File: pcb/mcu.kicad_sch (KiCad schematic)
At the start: 24 parts, among them J1 Conn_01x02_Pin, SW1 SW_Push, U1 STM32H750VBTx, U2 W25Q64JVSSIQ_C179171, U3 TLV1117LV33DCYR

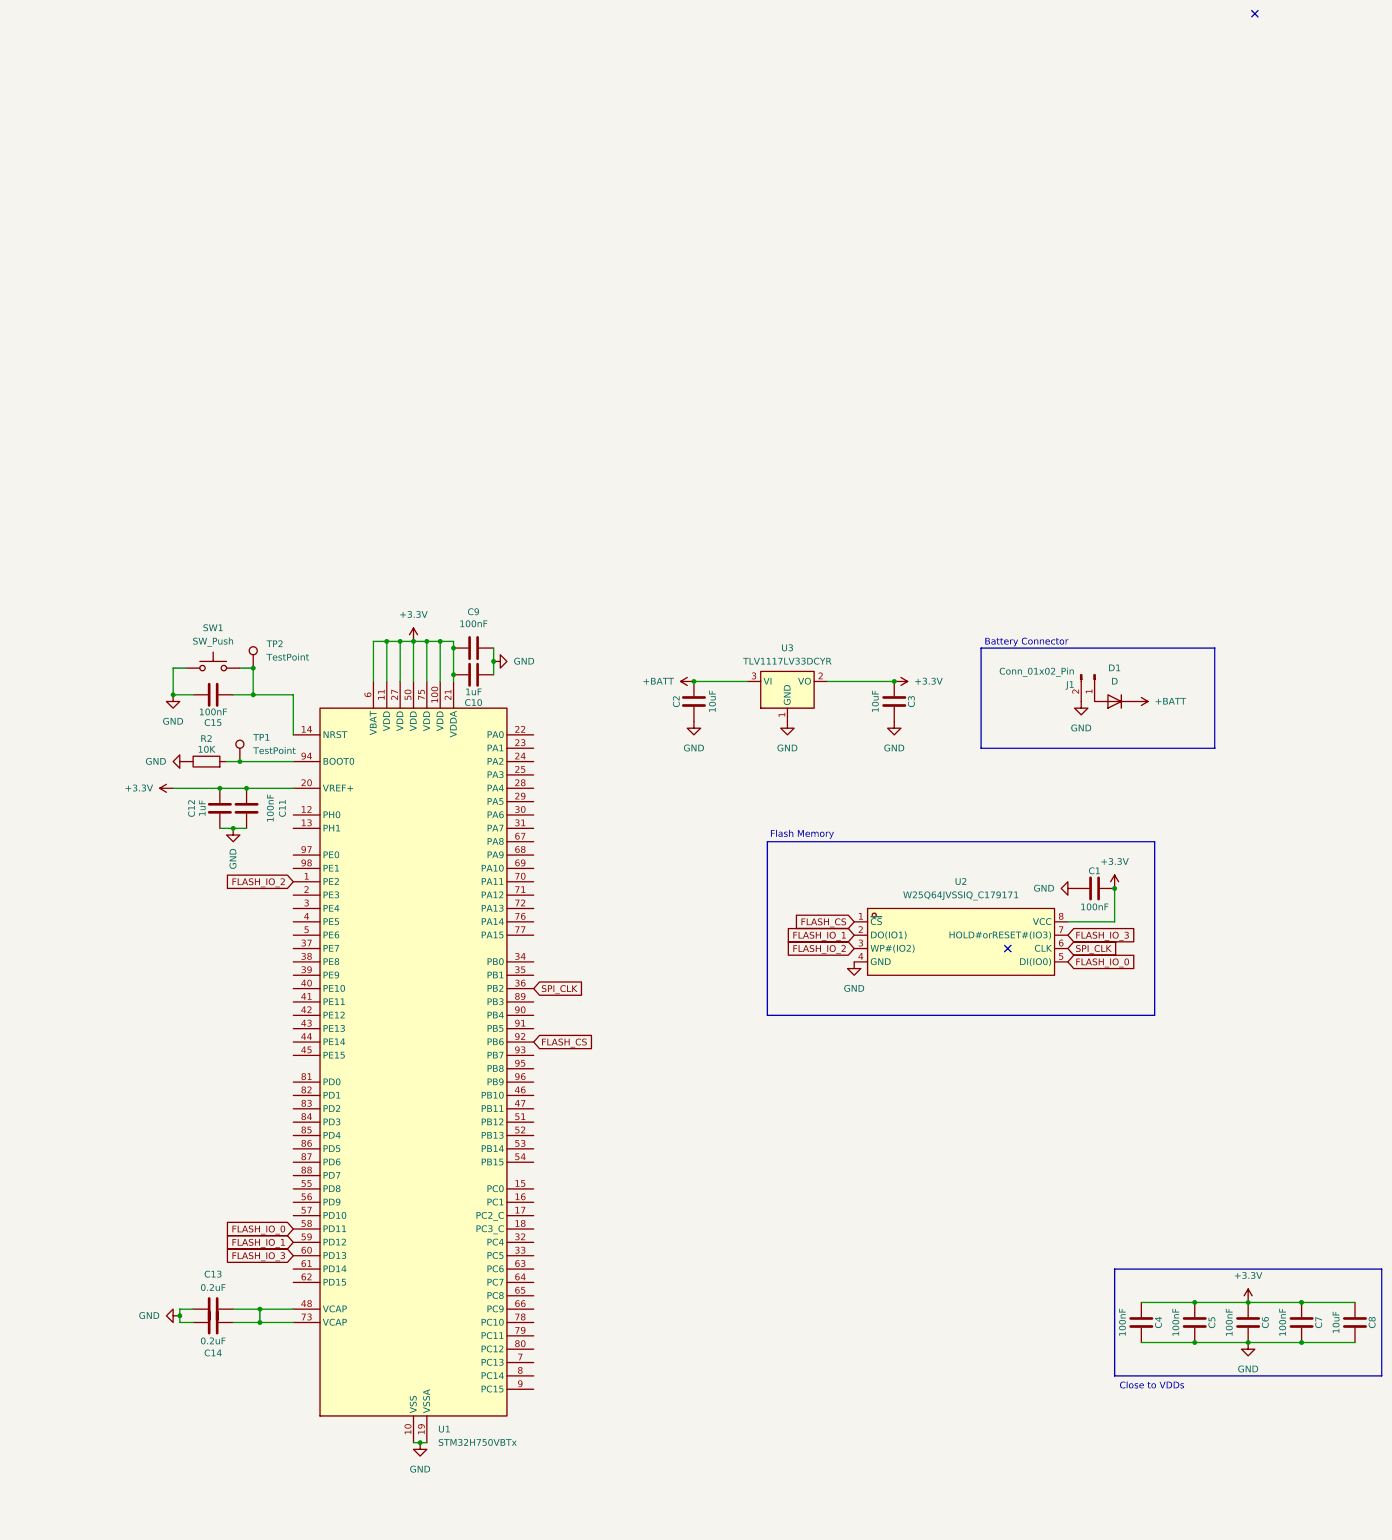
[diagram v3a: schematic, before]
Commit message: [pcb] motor controllers, label/group cleanup
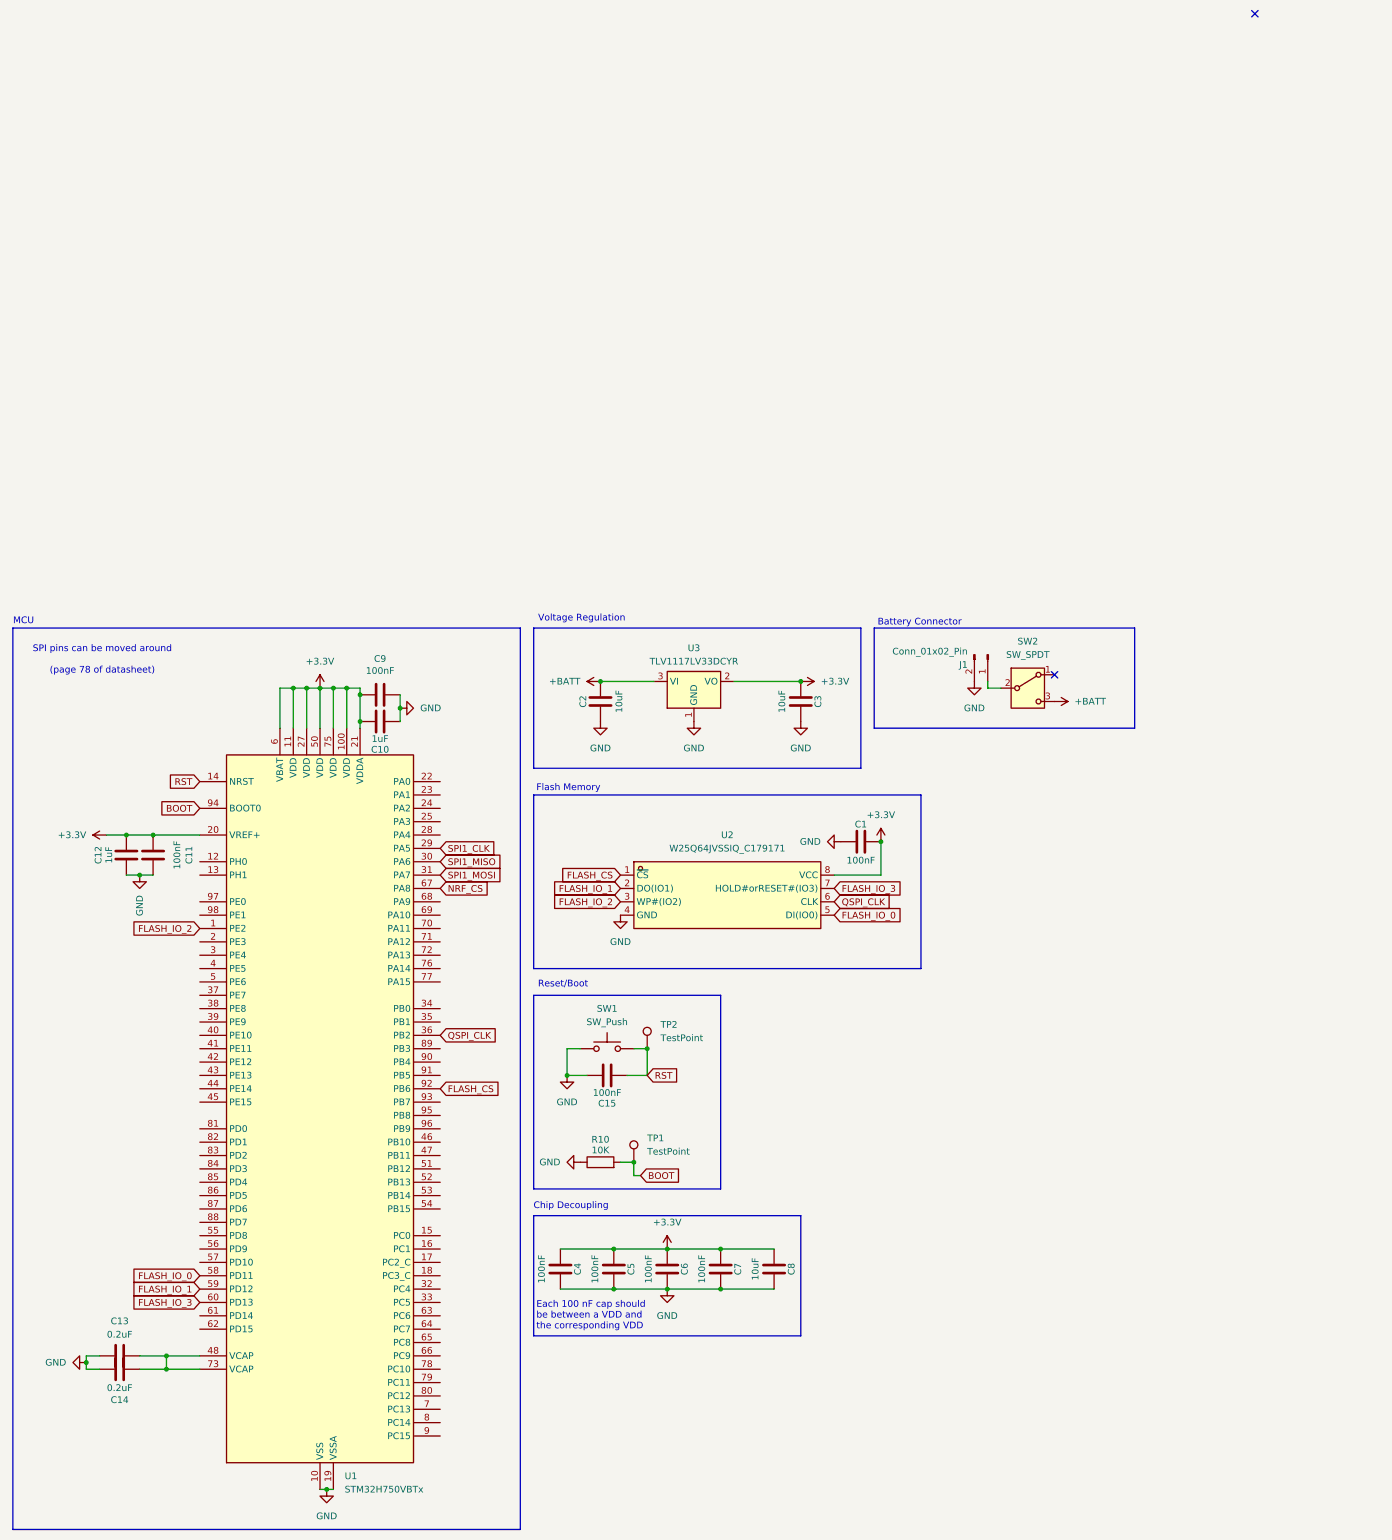
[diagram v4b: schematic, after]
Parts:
- removed D1: D, symbol Device:D
- removed R2: 10K, symbol Device:R
- added R10: 10K, symbol Device:R
- added SW2: SW_SPDT, symbol Switch:SW_SPDT
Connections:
- net +BATT: now also SW2.3 (C)
- net GND: now also R10.1
- net RST: now reaches C15.1, SW1.2, TP2.1, U1.14 (NRST)
- net BOOT: now reaches TP1.1, U1.94 (BOOT0)
- net BOOT: now also R10.2
- net at J1.1 (Pin_1): now also SW2.2 (B)
- net SPI1_CLK: now reaches U1.29 (PA5)
- net SPI1_MISO: now reaches U1.30 (PA6)
- net SPI1_MOSI: now reaches U1.31 (PA7)
- net NRF_CS: now reaches U1.67 (PA8)
- net SPI_CLK renamed QSPI_CLK
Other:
- note added: "Chip Decoupling"
- note added: "Each 100 nF cap should be between a VDD and the corresponding VDD"
- note added: "MCU"
- note added: "Reset/Boot"
- note added: "SPI pins can be moved around (page 78 of datasheet)"
- note added: "Voltage Regulation"
- note removed: "Close to VDDs"
- moved on the sheet: C1, C10, C11, C12, C13, C14, C15, C2, C3, C4, C5, C6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

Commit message: [pcb] improve MCU analog power, battery voltage measurement, JTAG header
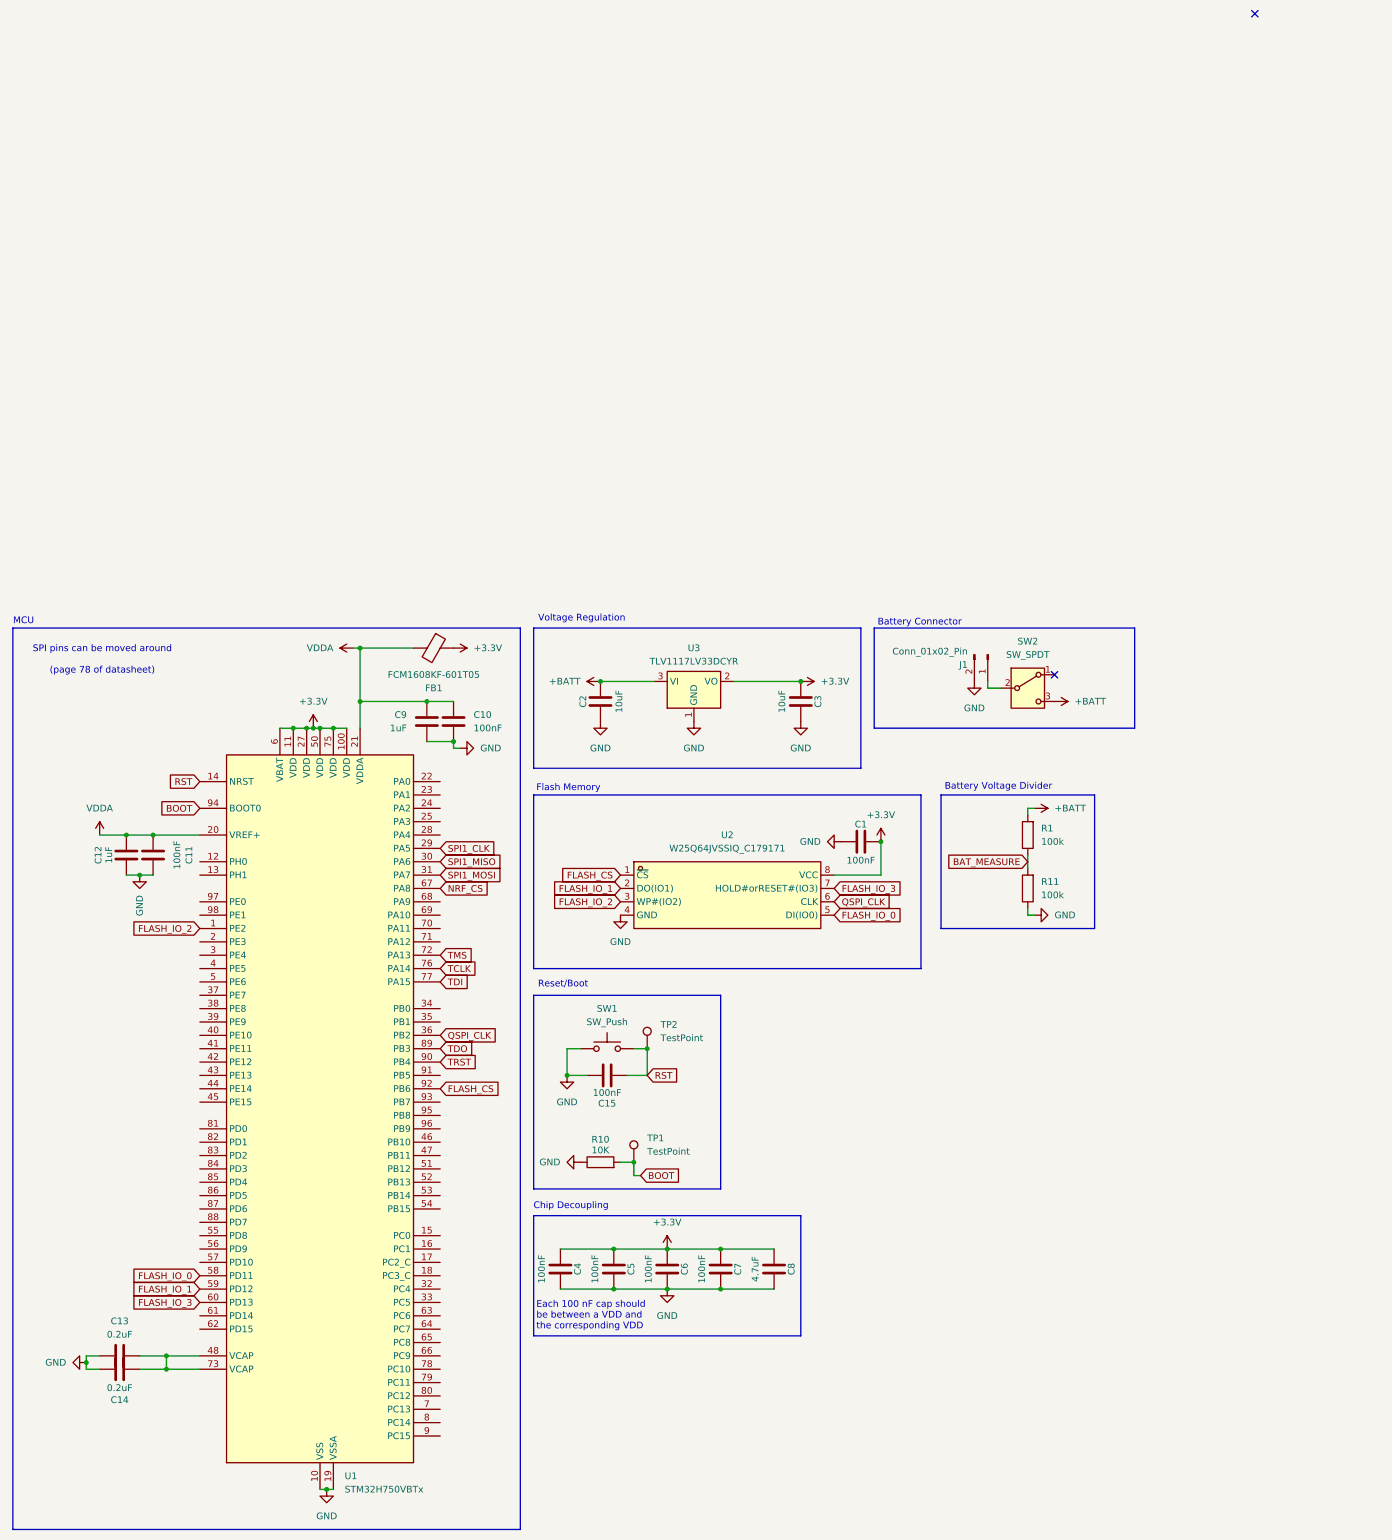
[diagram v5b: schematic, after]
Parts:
- added FB1: FCM1608KF-601T05, symbol Device:FerriteBead
- added R1, R11: 100k, symbol Device:R
- C10: value 1uF -> 100nF
- C8: value 10uF -> 4.7uF
- C9: value 100nF -> 1uF
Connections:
- net +3.3V: now also FB1.1; no longer C10.2, C11.1, C12.2, C9.1, U1.20 (VREF+), U1.21 (VDDA)
- net +BATT: now also R1.2
- net GND: now also C10.2, R11.1; no longer C10.1
- net TMS: now reaches U1.72 (PA13)
- net TCLK: now reaches U1.76 (PA14)
- net TDI: now reaches U1.77 (PA15)
- net TDO: now reaches U1.89 (PB3)
- net TRST: now reaches U1.90 (PB4)
- new net BAT_MEASURE: R1.1, R11.2
- new net VDDA: C10.1, C11.1, C12.2, C9.1, FB1.2, U1.20 (VREF+), U1.21 (VDDA)
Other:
- note added: "Battery Voltage Divider"

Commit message: [pcb] gpio selection, camera, crystal
- Each motors is connected to a channel of TIM1
- The battery voltage divider is connected to ADC1
- The NRF24 is connected to SPI2
- Added OV5640 camera (FPC connector) + LDOs
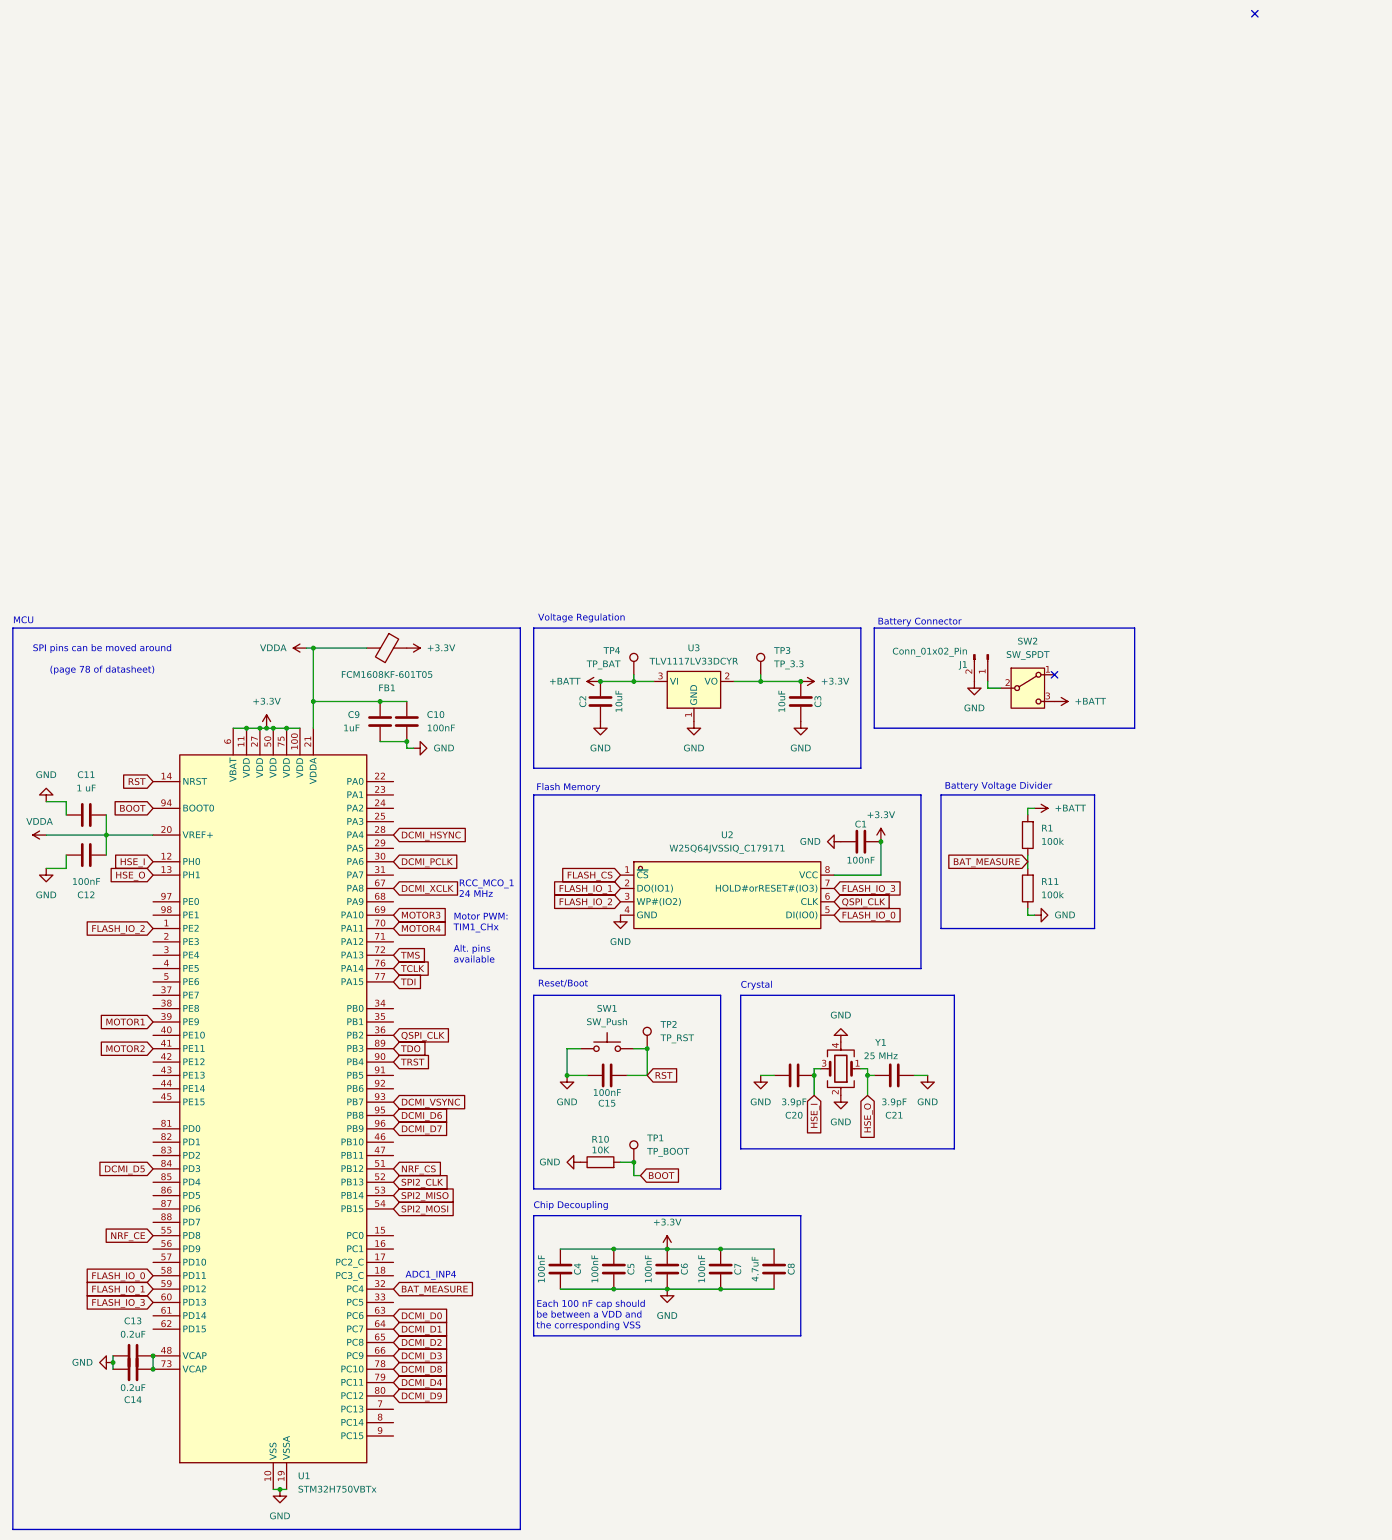
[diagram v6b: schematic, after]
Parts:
- added C20, C21: 3.9pF, symbol Device:C
- added TP3: TP_3.3, symbol Connector:TestPoint
- added TP4: TP_BAT, symbol Connector:TestPoint
- added Y1: 25 MHz, symbol Device:Crystal_GND24
- C11: value 100nF -> 1 uF
- C12: value 1uF -> 100nF
- TP1: value TestPoint -> TP_BOOT
- TP2: value TestPoint -> TP_RST
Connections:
- net +3.3V: now also TP3.1
- net +BATT: now also TP4.1
- net BAT_MEASURE: now also U1.32 (PC4)
- net FLASH_CS: no longer U1.92 (PB6)
- net GND: now also C11.1, C20.1, C21.2, Y1.2, Y1.4; no longer C11.2
- net NRF_CS: now also U1.51 (PB12); no longer U1.67 (PA8)
- net VDDA: now also C11.2; no longer C11.1
- net HSE_I: now reaches U1.12 (PH0)
- net HSE_I: now also C20.2, Y1.3
- net HSE_O: now reaches U1.13 (PH1)
- net HSE_O: now also C21.1, Y1.1
- net DCMI_HSYNC: now reaches U1.28 (PA4)
- net MOTOR1: now reaches U1.39 (PE9)
- net MOTOR2: now reaches U1.41 (PE11)
- net SPI2_CLK: now reaches U1.52 (PB13)
- net SPI2_MISO: now reaches U1.53 (PB14)
- net SPI2_MOSI: now reaches U1.54 (PB15)
- net NRF_CE: now reaches U1.55 (PD8)
- net DCMI_D0: now reaches U1.63 (PC6)
- net DCMI_D1: now reaches U1.64 (PC7)
- net DCMI_D2: now reaches U1.65 (PC8)
- net DCMI_D3: now reaches U1.66 (PC9)
- net MOTOR3: now reaches U1.69 (PA10)
- net MOTOR4: now reaches U1.70 (PA11)
- net DCMI_D8: now reaches U1.78 (PC10)
- net DCMI_D4: now reaches U1.79 (PC11)
- net DCMI_D9: now reaches U1.80 (PC12)
- net DCMI_D5: now reaches U1.84 (PD3)
- net DCMI_VSYNC: now reaches U1.93 (PB7)
- net DCMI_D6: now reaches U1.95 (PB8)
- net DCMI_D7: now reaches U1.96 (PB9)
- net SPI1_CLK: no longer names the net of U1.29 (PA5)
- net SPI1_MISO renamed DCMI_PCLK
- net SPI1_MOSI: no longer names the net of U1.31 (PA7)
- new net DCMI_XCLK: U1.67 (PA8)
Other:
- note added: "ADC1_INP4"
- note added: "Crystal"
- note added: "Each 100 nF cap should be between a VDD and the corresponding VSS"
- note added: "Motor PWM: TIM1_CHx Alt. pins available"
- note added: "RCC_MCO_1 24 MHz"
- note removed: "Each 100 nF cap should be between a VDD and the corresponding VDD"
- moved on the sheet: C10, C13, C14, C9, FB1, U1

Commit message: [pcb] add imu
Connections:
- net DCMI_D6: now also U1.4 (PE5); no longer U1.95 (PB8)
- net DCMI_D7: now also U1.5 (PE6); no longer U1.96 (PB9)
- net FLASH_CS: now also U1.92 (PB6)
- net IMU_SCL: now reaches U1.46 (PB10)
- net IMU_SDA: now reaches U1.47 (PB11)
- net DCMI_PWDN: now reaches U1.61 (PD14)
- net DCMI_RST: now reaches U1.62 (PD15)
- new net DCMI_SCL: U1.95 (PB8)
- new net DCMI_SDA: U1.96 (PB9)
